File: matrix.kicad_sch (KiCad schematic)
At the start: 156 parts, among them SW1 MX_SW_solder, SW10 MX_SW_solder, SW11 MX_SW_solder, SW12 MX_SW_solder, SW13 MX_SW_solder, SW14 MX_SW_solder, SW15 MX_SW_solder, SW16 MX_SW_solder, SW17 MX_SW_solder, SW18 MX_SW_solder, SW19 MX_SW_solder, SW2 MX_SW_solder, SW20 MX_SW_solder, SW21 MX_SW_solder, SW22 MX_SW_solder, SW23 MX_SW_solder, SW24 MX_SW_solder, SW25 MX_SW_solder, SW26 MX_SW_solder, SW27 MX_SW_solder, SW28 MX_SW_solder, SW29 MX_SW_solder, SW3 MX_SW_solder, SW30 MX_SW_solder, SW31 MX_SW_solder, SW32 MX_SW_solder, SW33 MX_SW_solder, SW34 MX_SW_solder, SW35 MX_SW_solder, SW36 MX_SW_solder, SW37 MX_SW_solder, SW38 MX_SW_solder, SW39 MX_SW_solder, SW4 MX_SW_solder, SW40 MX_SW_solder, SW41 MX_SW_solder, SW42 MX_SW_solder, SW43 MX_SW_solder, SW44 MX_SW_solder, SW45 MX_SW_solder, SW46 MX_SW_solder, SW47 MX_SW_solder, SW48 MX_SW_solder, SW49 MX_SW_solder, SW5 MX_SW_solder, SW50 MX_SW_solder, SW51 MX_SW_solder, SW52 MX_SW_solder, SW53 MX_SW_solder, SW54 MX_SW_solder, SW55 MX_SW_solder, SW56 MX_SW_solder, SW57 MX_SW_solder, SW58 MX_SW_solder, SW59 MX_SW_solder, SW6 MX_SW_solder, SW60 MX_SW_solder, SW61 MX_SW_solder, SW62 MX_SW_solder, SW63 MX_SW_solder, SW64 MX_SW_solder, SW65 MX_SW_solder, SW66 MX_SW_solder, SW67 MX_SW_solder, SW68 MX_SW_solder, SW69 MX_SW_solder, SW7 MX_SW_solder, SW70 MX_SW_solder, SW71 MX_SW_solder, SW72 MX_SW_solder, SW73 MX_SW_solder, SW74 MX_SW_solder, SW75 MX_SW_solder, SW76 MX_SW_solder, SW77 MX_SW_solder, SW78 MX_SW_solder, SW79 MX_SW_solder, SW8 MX_SW_solder, SW80 MX_SW_solder, SW81 MX_SW_solder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

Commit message: clean up
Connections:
- net at SW72.2: now also D71.2 (A), SW71.2, SW73.2
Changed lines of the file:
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@@
   (junction (at 157.48 121.92) (diameter 0) (color 0 0 0 0)
   )
+  (junction (at 118.11 137.16) (diameter 0) (color 0 0 0 0)
+  )
   (junction (at 215.9 137.16) (diameter 0) (color 0 0 0 0)
   )
@@
     (stroke (width 0) (type default) (color 0 0 0 0))
   )
-  (wire (pts (xy 118.11 154.94) (xy 118.11 121.92))
+  (wire (pts (xy 118.11 154.94) (xy 118.11 137.16))
     (stroke (width 0) (type default) (color 0 0 0 0))
   )
@@
     (stroke (width 0) (type default) (color 0 0 0 0))
   )
+  (wire (pts (xy 118.11 137.16) (xy 118.11 121.92))
+    (stroke (width 0) (type default) (color 0 0 0 0))
+  )
   (wire (pts (xy 119.38 55.88) (xy 119.38 76.2))
     (stroke (width 0) (type default) (color 0 0 0 0))
@@
     (stroke (width 0) (type default) (color 0 0 0 0))
   )
-  (wire (pts (xy 115.57 137.16) (xy 116.84 137.16))
-    (stroke (width 0) (type default) (color 0 0 0 0))
-  )
+  (wire (pts (xy 115.57 137.16) (xy 118.11 137.16))
+    (stroke (width 0) (type default) (color 0 0 0 0))
+  )

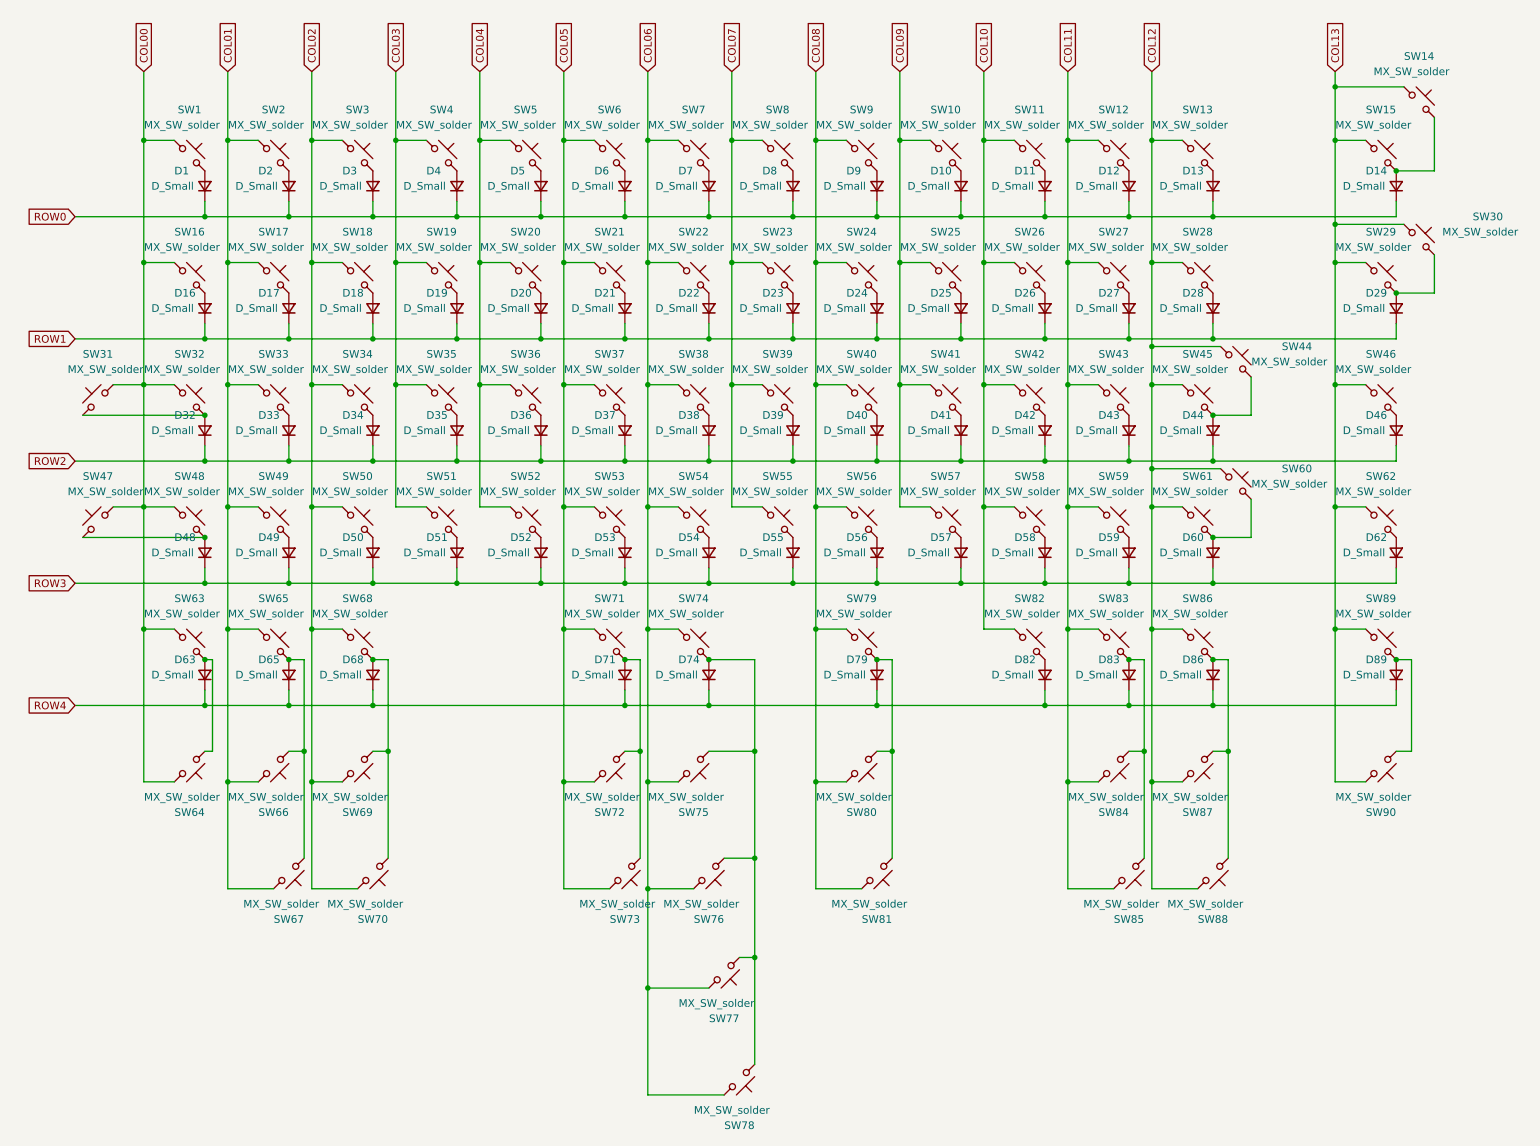
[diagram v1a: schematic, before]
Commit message: place switch and stab footprints
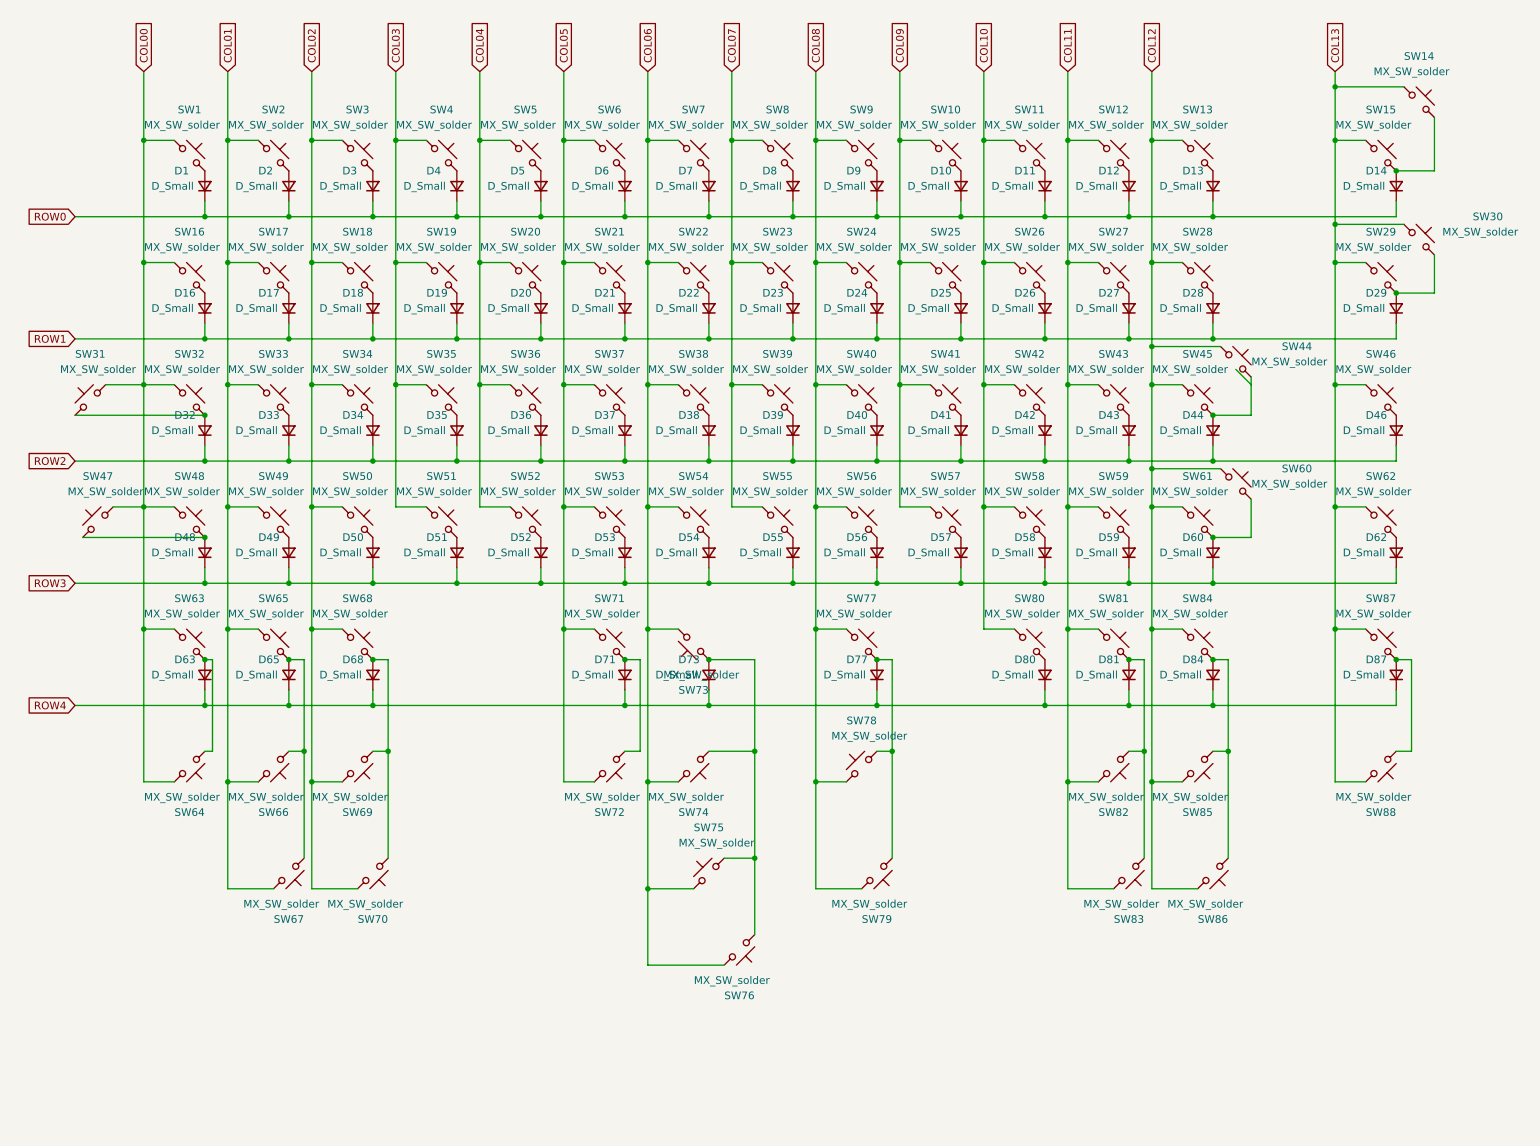
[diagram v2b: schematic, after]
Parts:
- removed SW73, SW77: MX_SW_solder, marbastlib-mx:SW_MX_1u, symbol marbastlib-mx:MX_SW_solder
- D1, D10, D11, D12, D13, D14, D16, D17, D18, D19, D2, D20, D21, D22, D23, D24, D25, D26, D27, D28, D29, D3, D32, D33, D34, D35, D36, D37, D38, D39, D4, D40, D41, D42, D43, D44, D46, D48, D49, D5, D50, D51, D52, D53, D54, D55, D56, D57, D58, D59, D6, D60, D62, D63, D65, D68, D7, D71, D8, D9: footprint (none) -> Diode_SMD:D_SOD-123
- D73: renamed from D74; footprint (none) -> Diode_SMD:D_SOD-123
- D77: renamed from D79; footprint (none) -> Diode_SMD:D_SOD-123
- D80: renamed from D82; footprint (none) -> Diode_SMD:D_SOD-123
- D81: renamed from D83; footprint (none) -> Diode_SMD:D_SOD-123
- D84: renamed from D86; footprint (none) -> Diode_SMD:D_SOD-123
- D87: renamed from D89; footprint (none) -> Diode_SMD:D_SOD-123
- SW16, SW29, SW64, SW69: footprint marbastlib-mx:SW_MX_1u -> marbastlib-mx:SW_MX_1.5u
- SW31: footprint marbastlib-mx:SW_MX_1u -> marbastlib-mx:SW_MX_1.75u_stp
- SW32, SW60: footprint marbastlib-mx:SW_MX_1u -> marbastlib-mx:SW_MX_1.75u
- SW47, SW63, SW65, SW67, SW68, SW70: footprint marbastlib-mx:SW_MX_1u -> marbastlib-mx:SW_MX_1.25u
- SW74: renamed from SW75; footprint marbastlib-mx:SW_MX_1u -> marbastlib-mx:SW_MX_1.25u
- SW76: renamed from SW78; footprint marbastlib-mx:SW_MX_1u -> marbastlib-mx:SW_MX_1.25u
- SW80: renamed from SW82; footprint marbastlib-mx:SW_MX_1u -> marbastlib-mx:SW_MX_1.25u
- SW81: renamed from SW83; footprint marbastlib-mx:SW_MX_1u -> marbastlib-mx:SW_MX_1.25u
- SW82: renamed from SW84; footprint marbastlib-mx:SW_MX_1u -> marbastlib-mx:SW_MX_1.5u
- SW83: renamed from SW85; footprint marbastlib-mx:SW_MX_1u -> marbastlib-mx:SW_MX_1.25u
- SW84: renamed from SW86; footprint marbastlib-mx:SW_MX_1u -> marbastlib-mx:SW_MX_1.25u
- SW86: renamed from SW88; footprint marbastlib-mx:SW_MX_1u -> marbastlib-mx:SW_MX_1.25u
- SW87: renamed from SW89; footprint marbastlib-mx:SW_MX_1u -> marbastlib-mx:SW_MX_1.25u
- SW88: renamed from SW90; footprint marbastlib-mx:SW_MX_1u -> marbastlib-mx:SW_MX_1.5u
- renumbered SW74 to SW73, SW76 to SW75, SW79 to SW77, SW80 to SW78, SW81 to SW79, SW87 to SW85
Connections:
- net COL06: now also SW73.2, SW75.2; no longer SW73.1, SW75.1
- net COL08: now also SW78.2; no longer SW78.1
- net at D73.2 (A), SW74.2, SW76.2: now also SW73.1, SW75.1; no longer SW73.2, SW75.2
- net at D77.2 (A), SW77.2, SW79.2: now also SW78.1; no longer SW78.2
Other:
- moved on the sheet: SW31, SW73, SW76

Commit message: flip some switches to simplify routing
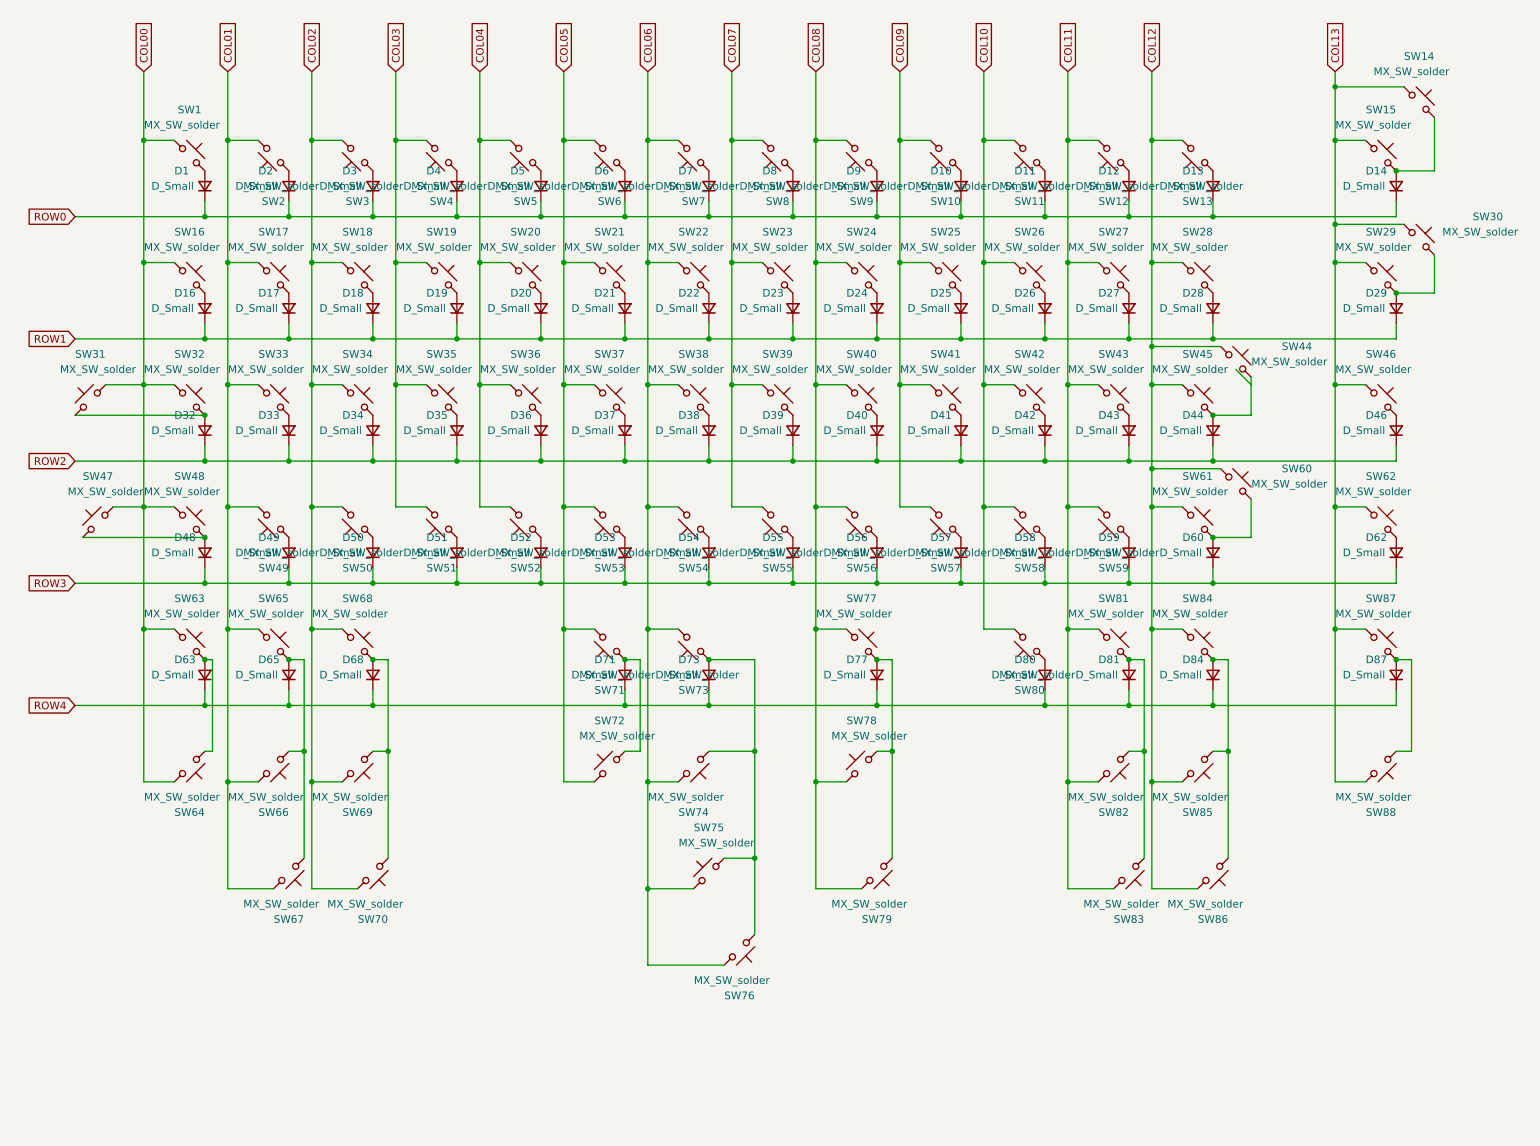
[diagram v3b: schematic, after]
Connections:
- net COL01: now also SW2.2, SW49.2; no longer SW2.1, SW49.1
- net COL02: now also SW3.2, SW50.2; no longer SW3.1, SW50.1
- net COL03: now also SW4.2, SW51.2; no longer SW4.1, SW51.1
- net COL04: now also SW5.2, SW52.2; no longer SW5.1, SW52.1
- net COL05: now also SW53.2, SW6.2, SW71.2, SW72.2; no longer SW53.1, SW6.1, SW71.1, SW72.1
- net COL06: now also SW54.2, SW7.2; no longer SW54.1, SW7.1
- net COL07: now also SW55.2, SW8.2; no longer SW55.1, SW8.1
- net COL08: now also SW56.2, SW9.2; no longer SW56.1, SW9.1
- net COL09: now also SW10.2, SW57.2; no longer SW10.1, SW57.1
- net COL10: now also SW11.2, SW58.2, SW80.2; no longer SW11.1, SW58.1, SW80.1
- net COL11: now also SW12.2, SW59.2; no longer SW12.1, SW59.1
- net COL12: now also SW13.2; no longer SW13.1
- net at D53.2 (A): now also SW53.1; no longer SW53.2
- net at D59.2 (A): now also SW59.1; no longer SW59.2
- net at D57.2 (A): now also SW57.1; no longer SW57.2
- net at D5.2 (A): now also SW5.1; no longer SW5.2
- net at D6.2 (A): now also SW6.1; no longer SW6.2
- net at D10.2 (A): now also SW10.1; no longer SW10.2
- net at D49.2 (A): now also SW49.1; no longer SW49.2
- net at D13.2 (A): now also SW13.1; no longer SW13.2
- net at D56.2 (A): now also SW56.1; no longer SW56.2
- net at D4.2 (A): now also SW4.1; no longer SW4.2
- net at D58.2 (A): now also SW58.1; no longer SW58.2
- net at D11.2 (A): now also SW11.1; no longer SW11.2
- net at D51.2 (A): now also SW51.1; no longer SW51.2
- net at D80.2 (A): now also SW80.1; no longer SW80.2
- net at D54.2 (A): now also SW54.1; no longer SW54.2
- net at D50.2 (A): now also SW50.1; no longer SW50.2
- net at D2.2 (A): now also SW2.1; no longer SW2.2
- net at D52.2 (A): now also SW52.1; no longer SW52.2
- net at D3.2 (A): now also SW3.1; no longer SW3.2
- net at D12.2 (A): now also SW12.1; no longer SW12.2
- net at D9.2 (A): now also SW9.1; no longer SW9.2
- net at D7.2 (A): now also SW7.1; no longer SW7.2
- net at D55.2 (A): now also SW55.1; no longer SW55.2
- net at D8.2 (A): now also SW8.1; no longer SW8.2
- new net: D71.2 (A), SW71.1, SW72.1
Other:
- moved on the sheet: SW10, SW11, SW12, SW13, SW2, SW3, SW4, SW49, SW5, SW50, SW51, SW52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
